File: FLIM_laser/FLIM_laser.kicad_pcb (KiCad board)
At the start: 2 copper layers, 18 parts, among them J1 Conn_01x02_Male, J2 Conn_01x02_Male, J3 Conn_01x02_Male, M1 EP2014C, U1 AMS1117-5.0, U2 LMG1020, U3 74LVC1G08

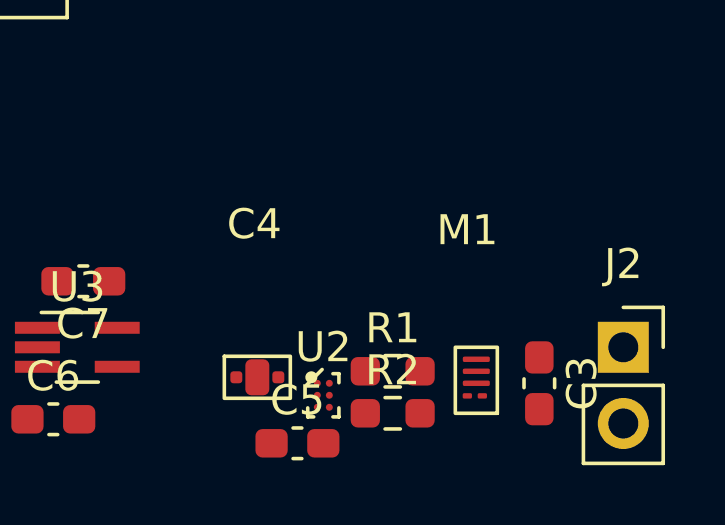
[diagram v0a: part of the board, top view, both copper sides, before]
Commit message: v0.8 footprints were corrected
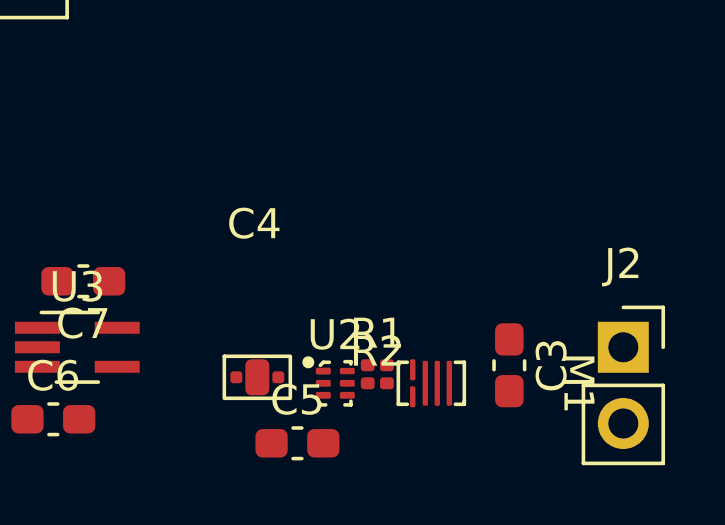
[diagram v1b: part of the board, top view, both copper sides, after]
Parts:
- R1, R2: footprint Resistor_SMD:R_0603_1608Metric_Pad0.98x0.95mm_HandSolder -> Resistor_SMD:R_0201_0603Metric
- U2: footprint FLIM_laser:BGA-6_2x3_0.8x1.2mm -> FLIM_laser:LMG1020
- moved M1 1.84 mm to (166.6, 50.0), turned to -90 degrees
- moved C3 1.17 mm to (169.8, 49.4)
- moved R2 1.12 mm to (165.4, 50.0)
- moved U2 0.57 mm to (164.0, 50.0)
- moved R1 0.55 mm to (165.4, 49.4)
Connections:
- M1 pad 1: +5V -> Net-(M1-Pad1)
- M1 pad 2: Net-(M1-Pad2) -> GND
- M1 pad 3: GND -> +5V
- M1 pad 5: (no net) -> +5V
- R1 pad 2: Net-(M1-Pad2) -> Net-(M1-Pad1)
- R2 pad 2: Net-(M1-Pad2) -> Net-(M1-Pad1)

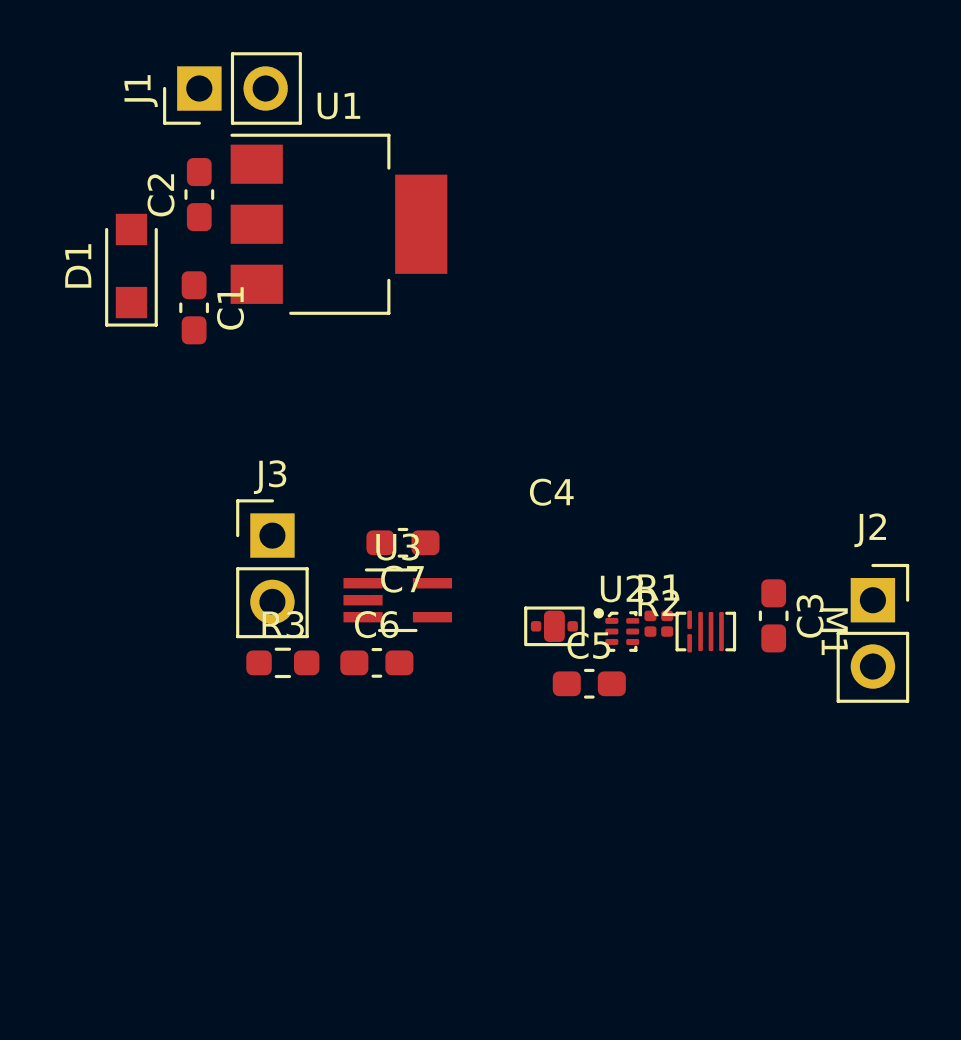
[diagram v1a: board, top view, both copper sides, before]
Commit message: v0.9 decomposition was completed
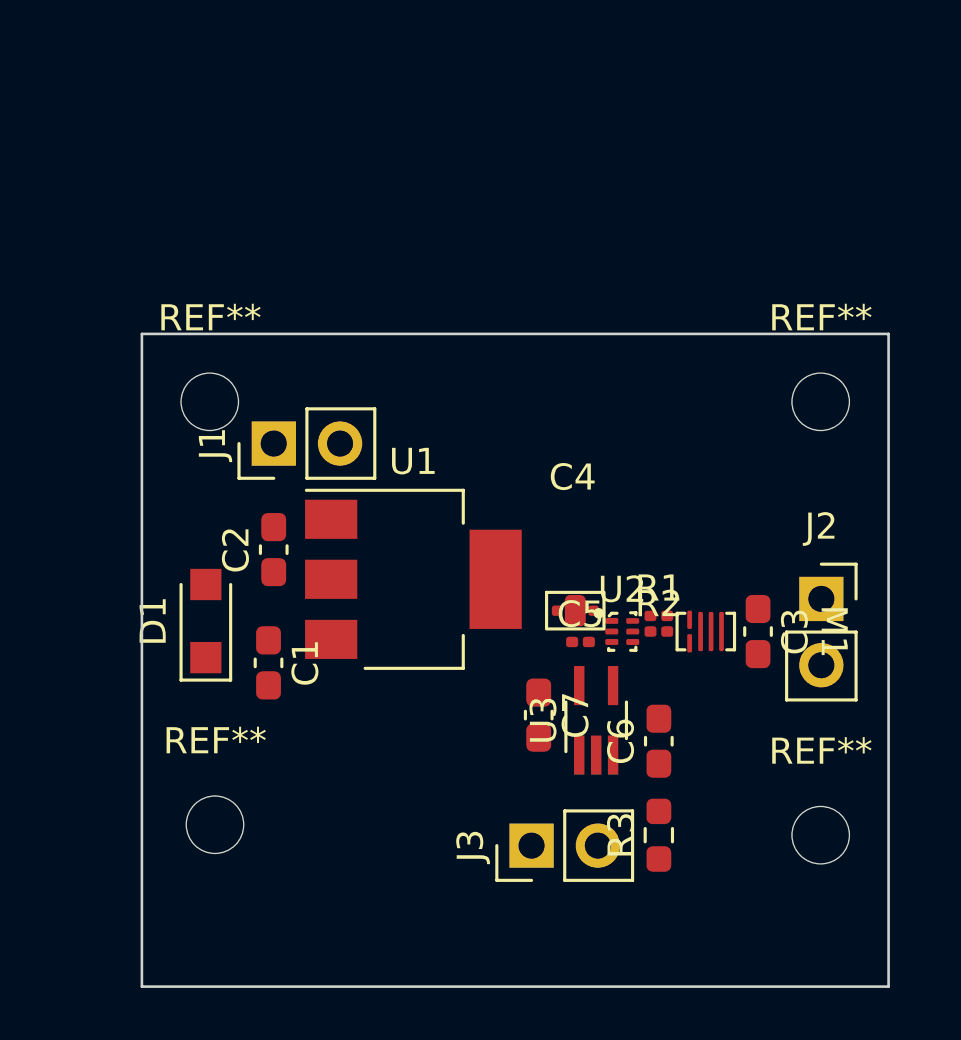
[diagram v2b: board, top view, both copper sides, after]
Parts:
- added REF**: MountingHole_2.2mm_M2, MountingHole:MountingHole_2.2mm_M2, F.Cu at (148.2, 41.2)
- added REF**: MountingHole_2.2mm_M2, MountingHole:MountingHole_2.2mm_M2, F.Cu at (171.6, 41.2)
- added REF**: MountingHole_2.2mm_M2, MountingHole:MountingHole_2.2mm_M2, F.Cu at (148.4, 57.4)
- added REF**: MountingHole_2.2mm_M2, MountingHole:MountingHole_2.2mm_M2, F.Cu at (171.6, 57.8)
- C5: footprint Capacitor_SMD:C_0603_1608Metric_Pad1.08x0.95mm_HandSolder -> Capacitor_SMD:C_0201_0603Metric
- moved R3 15.8 mm to (165.4, 57.8), turned to 90 degrees
- moved J3 15.5 mm to (160.5, 58.2), turned to 90 degrees
- moved D1 13.9 mm to (148.1, 49.6)
- moved C1 13.9 mm to (150.4, 51.2)
- moved U1 13.9 mm to (156.0, 48.0)
- moved J1 13.9 mm to (150.7, 42.8)
- moved C2 13.9 mm to (150.7, 46.9)
- moved C6 11.2 mm to (165.4, 54.2), turned to 90 degrees
- moved U3 8.88 mm to (163.0, 53.4), turned to 90 degrees
- moved C7 8.40 mm to (160.8, 53.2), turned to -90 degrees
- moved J2 1.98 mm to (171.6, 48.8)
- moved C5 1.64 mm to (162.4, 50.4)
- moved C4 1.00 mm to (162.2, 49.2)
- moved C3 0.85 mm to (169.2, 50.0)
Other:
- board outline added: 28.6 x 25 mm

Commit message: v0.92 subcompleted
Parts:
- added J4: Conn_01x02_Male, Connector_PinHeader_2.54mm:PinHeader_1x02_P2.54mm_Vertical, F.Cu at (162.6, 59.2)
- added R4: R, Resistor_SMD:R_0603_1608Metric_Pad0.98x0.95mm_HandSolder, F.Cu at (165.5, 56.6)
- J1, J3: footprint Connector_PinHeader_2.54mm:PinHeader_1x02_P2.54mm_Vertical -> Connector_PinSocket_2.54mm:PinSocket_1x02_P2.54mm_Vertical
- J2: footprint Connector_PinSocket_2.54mm:PinSocket_1x02_P2.54mm_Vertical -> Connector_PinHeader_2.54mm:PinHeader_1x02_P2.54mm_Vertical
- R1: footprint Resistor_SMD:R_0201_0603Metric -> Resistor_SMD:R_0603_1608Metric_Pad0.98x0.95mm_HandSolder
- R3: footprint Resistor_SMD:R_0603_1608Metric_Pad0.98x0.95mm_HandSolder -> Resistor_SMD:R_0201_0603Metric
- moved J2 21.9 mm to (150.6, 42.8), turned to 90 degrees
- moved J1 17.7 mm to (168.2, 45.4)
- moved J3 14.3 mm to (172.2, 50.0), turned to 0 degrees
- moved R3 7.60 mm to (165.5, 50.2), turned to 0 degrees
- moved C6 3.89 mm to (162.3, 56.6), turned to 180 degrees
- moved REF** 3.41 mm to (148.6, 60.8)
- moved REF** 3.03 mm to (171.2, 60.8)
- moved R1 2.13 mm to (167.0, 48.0)
- moved C3 1.02 mm to (169.4, 51.0)
- moved D1 0.97 mm to (148.6, 48.8)
- moved R2 0.62 mm to (165.5, 49.4)
- moved M1 0.28 mm to (166.8, 50.2)
- moved REF** 0.28 mm to (148.4, 41.4)
- moved REF** 0.28 mm to (171.4, 41.4)
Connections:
- C3 pad 1: +5V -> Net-(C3-Pad1)
- J1 pad 1: Net-(D1-Pad2) -> Net-(C3-Pad1)
- J2 pad 1: +5V -> Net-(D1-Pad2)
- J3 pad 1: Net-(J3-Pad1) -> Net-(C3-Pad1)
- J3 pad 2: Net-(J3-Pad2) -> GND
- M1 pad 3: +5V -> Net-(C3-Pad1)
- M1 pad 5: +5V -> Net-(C3-Pad1)
- R1 pad 1: Net-(R1-Pad1) -> +5V
- R1 pad 2: Net-(M1-Pad1) -> Net-(C3-Pad1)
- R3 pad 1: Net-(J3-Pad2) -> Net-(R3-Pad1)
- R3 pad 2: Net-(C6-Pad1) -> Net-(M1-Pad1)
- U2 pad A2: Net-(R1-Pad1) -> Net-(R2-Pad1)
- U2 pad B2: Net-(R2-Pad1) -> Net-(R3-Pad1)
- U3 pad 1: Net-(J3-Pad1) -> Net-(J4-Pad1)
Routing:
- net +5V: track 0.00 -> 22.3 mm
- net Net-(C3-Pad1): track 0.00 -> 18.8 mm
- net Net-(D1-Pad2): track 0.00 -> 5.43 mm
- net Net-(J4-Pad1): track 0.00 -> 4.59 mm
- net Net-(C1-Pad1): track 0.00 -> 4.57 mm
- net Net-(C6-Pad1): track 0.00 -> 3.35 mm
- net Net-(J4-Pad2): track 0.00 -> 3.13 mm
- net Net-(U2-PadC1): track 0.00 -> 1.58 mm
- net Net-(C4-Pad3): track 0.00 -> 0.87 mm
- net Net-(M1-Pad1): track 0.00 -> 0.80 mm
- net GND: vias 0 -> 26
- added copper zone on B.Cu, net GND
- added copper zone on F.Cu, net GND

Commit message: v0.93 subcomplected 2
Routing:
- net Net-(M1-Pad1): track 0.80 -> 4.93 mm
- net GND: track 0.00 -> 3.59 mm
- net +5V: track 22.3 -> 23.9 mm
- net Net-(R3-Pad1): track 0.00 -> 0.55 mm
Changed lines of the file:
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@@
   (segment (start 149.4 50.2) (end 149.6 50.4) (width 0.8) (layer "F.Cu") (net 1))
   (segment (start 150.3125 50.2) (end 150.45 50.3375) (width 0.25) (layer "F.Cu") (net 1))
+  (segment (start 166.78 50.65) (end 166.78 51.38) (width 0.2) (layer "F.Cu") (net 2))
+  (segment (start 166.8 51.4) (end 167.6 51.4) (width 0.2) (layer "F.Cu") (net 2))
+  (segment (start 162.72 50.08) (end 162.8 50) (width 0.2) (layer "F.Cu") (net 2))
+  (segment (start 162.72 50.4) (end 162.72 50.08) (width 0.2) (layer "F.Cu") (net 2))
+  (segment (start 167.6 51.4) (end 167.6 50.2) (width 0.2) (layer "F.Cu") (net 2))
+  (segment (start 162.8 50) (end 163.2 50) (width 0.2) (layer "F.Cu") (net 2))
+  (segment (start 166.78 51.38) (end 166.8 51.4) (width 0.2) (layer "F.Cu") (net 2))
   (via (at 161.2 44.4) (size 0.8) (drill 0.4) (layers "F.Cu" "B.Cu") (free) (net 2))
   (via (at 156.6 40.2) (size 0.8) (drill 0.4) (layers "F.Cu" "B.Cu") (free) (net 2))
@@
   (segment (start 159.75 47.4) (end 159.15 48) (width 1) (layer "F.Cu") (net 3))
   (segment (start 162.0825 52.3375) (end 162.35 52.07) (width 0.25) (layer "F.Cu") (net 3))
-  (segment (start 162.08 50.4) (end 162 50.4) (width 0.25) (layer "F.Cu") (net 3))
   (segment (start 166.0875 48) (end 165.98798 47.90048) (width 1) (layer "F.Cu") (net 3))
+  (segment (start 161.4 49.20048) (end 161.40048 49.2) (width 0.25) (layer "F.Cu") (net 3))
+  (segment (start 161.8 50.4) (end 161.4 50) (width 0.25) (layer "F.Cu") (net 3))
+  (segment (start 161.4 50) (end 161.4 49.20048) (width 0.25) (layer "F.Cu") (net 3))
+  (segment (start 162.08 50.4) (end 161.8 50.4) (width 0.25) (layer "F.Cu") (net 3))
   (segment (start 159.8 49.2) (end 159.15 48.55) (width 0.25) (layer "F.Cu") (net 3))
   (segment (start 160.8 52.3375) (end 162.0825 52.3375) (width 0.25) (layer "F.Cu") (net 3))
@@
   (segment (start 163.65 50.56452) (end 163.6 50.51452) (width 0.4) (layer "F.Cu") (net 8))
   (segment (start 163.65 52.07) (end 163.65 50.56452) (width 0.4) (layer "F.Cu") (net 8))
-  (segment (start 165.865 49.4) (end 165.865 50.2) (width 0.4) (layer "F.Cu") (net 9))
+  (segment (start 166.77 49.4) (end 166.77 49.75) (width 0.2) (layer "F.Cu") (net 9))
+  (segment (start 165.865 49.4) (end 165.865 49.935) (width 0.4) (layer "F.Cu") (net 9))
+  (segment (start 166.2 49.8) (end 166.1 49.7) (width 0.3) (layer "F.Cu") (net 9))
+  (segment (start 166.72 49.69) (end 166.72 49.81) (width 0.3) (layer "F.Cu") (net 9))
+  (segment (start 165.865 49.4) (end 166 49.4) (width 0.3) (layer "F.Cu") (net 9))
+  (segment (start 166.595 49.935) (end 165.865 49.935) (width 0.3) (layer "F.Cu") (net 9))
+  (segment (start 165.865 49.935) (end 166.1 49.7) (width 0.3) (layer "F.Cu") (net 9))
+  (segment (start 166.2 49.6) (end 166.63 49.6) (width 0.3) (layer "F.Cu") (net 9))
+  (segment (start 165.865 49.4) (end 166.77 49.4) (width 0.2) (layer "F.Cu") (net 9))
+  (segment (start 166.72 49.81) (end 166.595 49.935) (width 0.3) (layer "F.Cu") (net 9))
+  (segment (start 166 49.4) (end 166.2 49.6) (width 0.3) (layer "F.Cu") (net 9))
+  (segment (start 166.63 49.6) (end 166.72 49.69) (width 0.3) (layer "F.Cu") (net 9))
+  (segment (start 165.865 49.935) (end 165.865 50.2) (width 0.4) (layer "F.Cu") (net 9))
+  (segment (start 166.6 49.8) (end 166.2 49.8) (width 0.3) (layer "F.Cu") (net 9))
   (segment (start 167.8 48.6) (end 167.8 48.8) (width 0.2) (layer "F.Cu") (net 10))
   (segment (start 168 49) (end 168 48.8) (width 0.2) (layer "F.Cu") (net 10))
@@
   (segment (start 169.4 49.2) (end 169.4 50.1375) (width 0.8) (layer "F.Cu") (net 10))
   (segment (start 168 48.8) (end 168 48.0875) (width 0.2) (layer "F.Cu") (net 10))
+  (segment (start 164.892011 50.042989) (end 164.797891 50.042989) (width 0.2) (layer "F.Cu") (net 11))
+  (segment (start 164.954902 50.2) (end 164.892011 50.137109) (width 0.2) (layer "F.Cu") (net 11))
+  (segment (start 165.225 50.2) (end 164.954902 50.2) (width 0.2) (layer "F.Cu") (net 11))
+  (segment (start 164.892011 50.137109) (end 164.892011 50.042989) (width 0.2) (layer "F.Cu") (net 11))
   (segment (start 162.35 58.95) (end 162.35 54.73) (width 0.2) (layer "F.Cu") (net 12))
   (segment (start 162.33702 54.74298) (end 162.35 54.73) (width 0.25) (layer "F.Cu") (net 12))

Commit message: v0.94 something
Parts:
- moved C3 0.20 mm to (169.6, 51.0)
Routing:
- net Net-(C3-Pad1): track 18.8 -> 22.5 mm
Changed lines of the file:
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@@
   )
   (footprint "Capacitor_SMD:C_0603_1608Metric_Pad1.08x0.95mm_HandSolder" (layer "F.Cu")
-    (at 169.4 51 -90)
+    (at 169.6 51 -90)
     (descr "Capacitor SMD 0603 (1608 Metric), square (rectangular) end terminal, IPC_7351 nominal with elongated pad for handsoldering. (Body size source: IPC-SM-782 page 76, https://www.pcb-3d.com/wordpress/wp-content/uploads/ipc-sm-782a_amendment_1_and_2.pdf), generated with kicad-footprint-generator")
     (tags "capacitor handsolder")
@@
   (segment (start 166.6 49.8) (end 166.2 49.8) (width 0.3) (layer "F.Cu") (net 9))
   (segment (start 167.8 48.6) (end 167.8 48.8) (width 0.2) (layer "F.Cu") (net 10))
+  (segment (start 167.8 48.6) (end 169.2 48.6) (width 0.6) (layer "F.Cu") (net 10))
   (segment (start 168 49) (end 168 48.8) (width 0.2) (layer "F.Cu") (net 10))
   (segment (start 167.8 48.1125) (end 167.9125 48) (width 0.2) (layer "F.Cu") (net 10))
+  (segment (start 169.6 50.1375) (end 172.0625 50.1375) (width 0.8) (layer "F.Cu") (net 10))
   (segment (start 168.2 45.4) (end 168.2 46.2) (width 0.6) (layer "F.Cu") (net 10))
   (segment (start 167.9125 48) (end 167.9125 48.0875) (width 0.2) (layer "F.Cu") (net 10))
@@
   (segment (start 167.6 48.6) (end 167.8 48.6) (width 0.2) (layer "F.Cu") (net 10))
   (segment (start 168.2 46.2) (end 168 46.4) (width 0.6) (layer "F.Cu") (net 10))
-  (segment (start 168.8 48.6) (end 169.4 49.2) (width 0.8) (layer "F.Cu") (net 10))
+  (segment (start 172.0625 50.1375) (end 172.2 50) (width 0.8) (layer "F.Cu") (net 10))
   (segment (start 167.9125 48.0875) (end 167.6 48.4) (width 0.2) (layer "F.Cu") (net 10))
+  (segment (start 167.9125 48) (end 167.9125 48.45) (width 0.8) (layer "F.Cu") (net 10))
   (segment (start 167.4 49) (end 168 49) (width 0.2) (layer "F.Cu") (net 10))
   (segment (start 167.4 48.8) (end 167.4 48.4) (width 0.2) (layer "F.Cu") (net 10))
+  (segment (start 168 49) (end 169.6 49) (width 0.6) (layer "F.Cu") (net 10))
   (segment (start 167.18856 49.15048) (end 167.95048 49.15048) (width 0.2) (layer "F.Cu") (net 10))
   (segment (start 168 48.8) (end 167.8 48.8) (width 0.2) (layer "F.Cu") (net 10))
+  (segment (start 169.6 49) (end 169.6 50.1375) (width 0.6) (layer "F.Cu") (net 10))
   (segment (start 167.95048 49.15048) (end 168 49.2) (width 0.2) (layer "F.Cu") (net 10))
   (segment (start 168 50.2) (end 168 49.2) (width 0.2) (layer "F.Cu") (net 10))
@@
   (segment (start 167.6 48.6) (end 167.4 48.8) (width 0.2) (layer "F.Cu") (net 10))
   (segment (start 167.16952 49.16952) (end 167.18856 49.15048) (width 0.2) (layer "F.Cu") (net 10))
-  (segment (start 168.5125 48.6) (end 168.8 48.6) (width 0.8) (layer "F.Cu") (net 10))
-  (segment (start 169.4 50.1375) (end 172.0625 50.1375) (width 0.8) (layer "F.Cu") (net 10))
   (segment (start 168 49.2) (end 168 49) (width 0.2) (layer "F.Cu") (net 10))
   (segment (start 167.16952 50.16952) (end 167.2 50.2) (width 0.2) (layer "F.Cu") (net 10))
   (segment (start 168 46.4) (end 167.9125 46.4875) (width 0.8) (layer "F.Cu") (net 10))
   (segment (start 167.4 48.8) (end 167.3 48.9) (width 0.2) (layer "F.Cu") (net 10))
-  (segment (start 167.9125 48) (end 168.5125 48.6) (width 0.8) (layer "F.Cu") (net 10))
   (segment (start 167.8 48.8) (end 167.4 48.8) (width 0.2) (layer "F.Cu") (net 10))
   (segment (start 167.3 48.9) (end 167.4 49) (width 0.2) (layer "F.Cu") (net 10))
   (segment (start 167.3 48.9) (end 167.16952 49.03048) (width 0.2) (layer "F.Cu") (net 10))
-  (segment (start 172.0625 50.1375) (end 172.2 50) (width 0.8) (layer "F.Cu") (net 10))
+  (segment (start 168.6 48) (end 169.3 48.7) (width 0.6) (layer "F.Cu") (net 10))
   (segment (start 167.9125 48.4875) (end 167.8 48.6) (width 0.2) (layer "F.Cu") (net 10))
+  (segment (start 167.9125 48) (end 168.6 48) (width 0.6) (layer "F.Cu") (net 10))
+  (segment (start 169.3 48.7) (end 169.6 49) (width 0.6) (layer "F.Cu") (net 10))
   (segment (start 167.16952 49.03048) (end 167.16952 49.16952) (width 0.2) (layer "F.Cu") (net 10))
   (segment (start 168 48.0875) (end 167.9125 48) (width 0.2) (layer "F.Cu") (net 10))
@@
   (segment (start 167.9125 46.4875) (end 167.9125 48) (width 0.8) (layer "F.Cu") (net 10))
   (segment (start 167.4 48.4) (end 167.8 48) (width 0.2) (layer "F.Cu") (net 10))
-  (segment (start 169.4 49.2) (end 169.4 50.1375) (width 0.8) (layer "F.Cu") (net 10))
   (segment (start 168 48.8) (end 168 48.0875) (width 0.2) (layer "F.Cu") (net 10))
+  (segment (start 169.2 48.6) (end 169.3 48.7) (width 0.6) (layer "F.Cu") (net 10))
   (segment (start 164.892011 50.042989) (end 164.797891 50.042989) (width 0.2) (layer "F.Cu") (net 11))
   (segment (start 164.954902 50.2) (end 164.892011 50.137109) (width 0.2) (layer "F.Cu") (net 11))

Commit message: v0.95 DRC was conducted
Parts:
- moved J2 2.33 mm to (152.9, 42.6)
- moved C7 0.20 mm to (160.8, 53.4)
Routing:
- net +5V: track 23.9 -> 28.2 mm
- net Net-(D1-Pad2): track 5.43 -> 6.90 mm
- net Net-(R2-Pad1): track 0.00 -> 0.91 mm
